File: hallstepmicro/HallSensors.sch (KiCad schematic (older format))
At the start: 16 parts

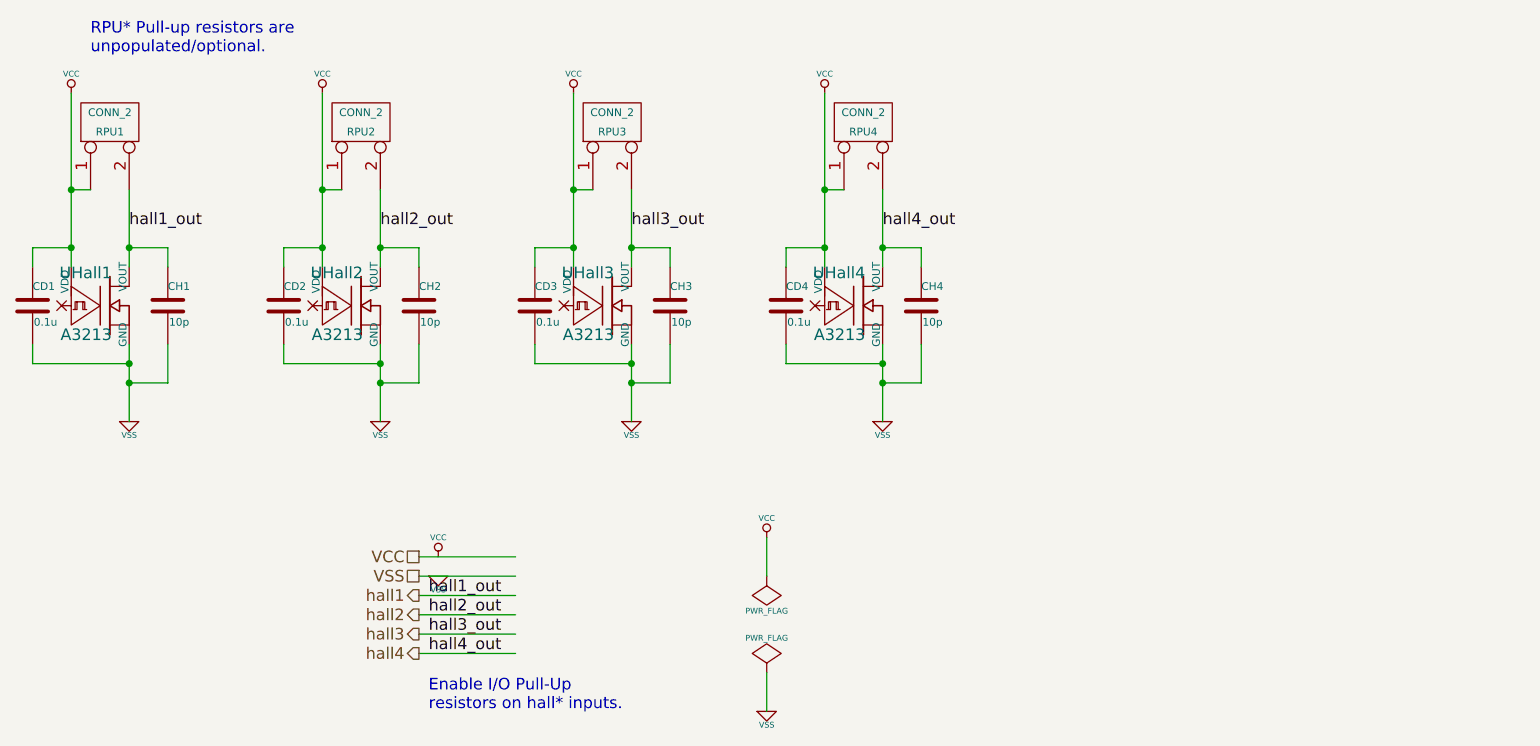
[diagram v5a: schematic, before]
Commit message: Adding some documentation & related markup.
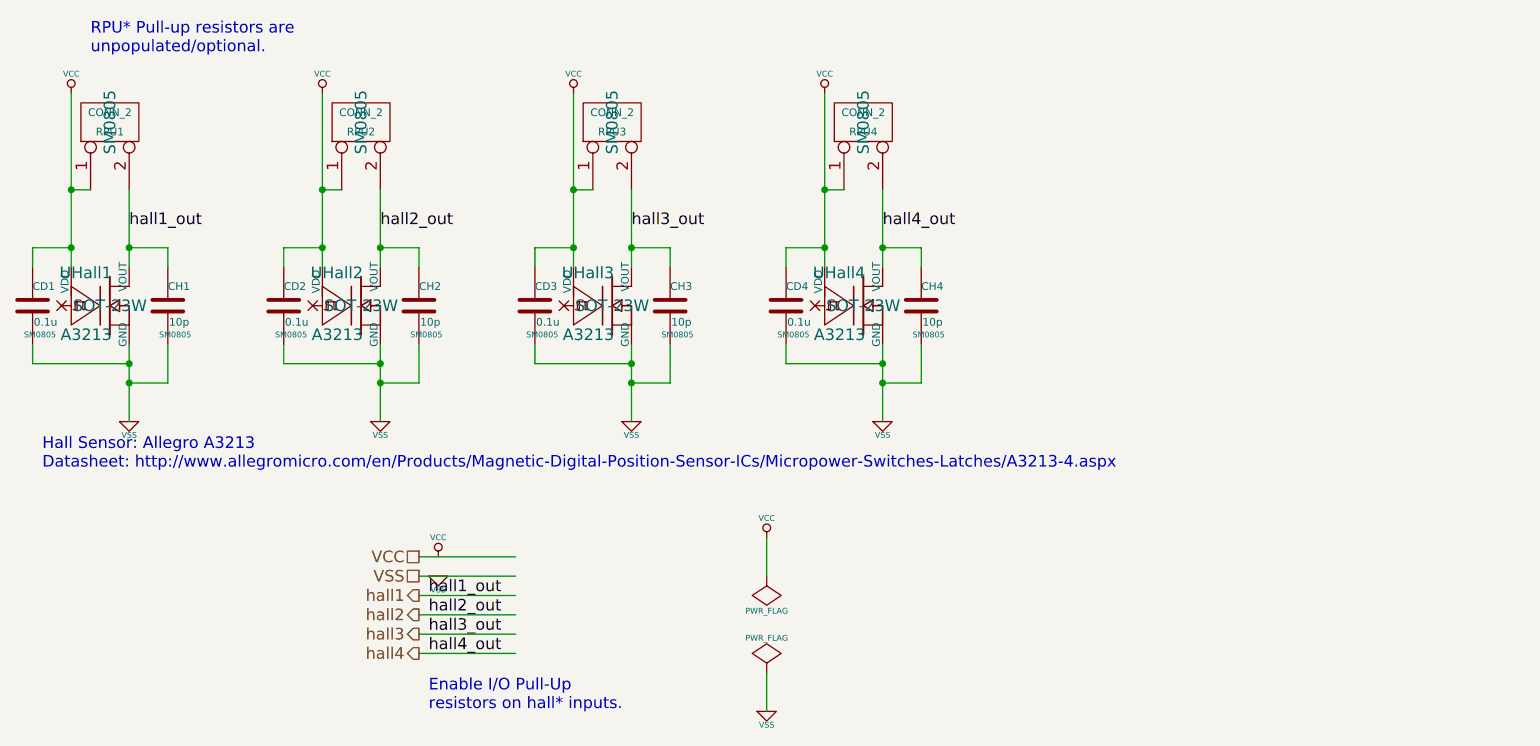
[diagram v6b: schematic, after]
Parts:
- CD1, CD2, CD3, CD4, CH1, CH2, CH3, CH4: footprint ~ -> SM0805
- RPU1, RPU2, RPU3, RPU4: footprint (none) -> SM0805
- UHall1, UHall2, UHall3, UHall4: footprint ~ -> SOT-23W
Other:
- note added: "Hall Sensor: Allegro A3213\nDatasheet: http://www.allegromicro.com/en/Products/Magnetic-Digital-Position-Sensor-ICs/Micropower-Switches-Latches/A3213-4.aspx"
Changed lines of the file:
@@
-EESchema Schematic File Version 2  date Wednesday, 02 October, 2013 09:18:38 pm
+EESchema Schematic File Version 2  date Friday, 04 October, 2013 11:24:01 am
 LIBS:power
 LIBS:device
@@
 encoding utf-8
 Sheet 2 2
-Title ""
-Date "3 oct 2013"
-Rev ""
-Comp ""
+Title "Hall Sensors With ATtiny84A Support"
+Date "4 oct 2013"
+Rev "20131004"
+Comp "ClothBot Designs"
 Comment1 ""
 Comment2 ""
@@
 F 0 "UHall1" H 1710 3670 60  0000 R CNN
 F 1 "A3213" H 1710 3350 60  0000 R CNN
-F 2 "~" H 1700 3500 60  0000 C CNN
-F 3 "~" H 1700 3500 60  0000 C CNN
+F 2 "SOT-23W" H 1700 3500 60  0000 C CNN
+F 3 "http://www.allegromicro.com/en/Products/Magnetic-Digital-Position-Sensor-ICs/Micropower-Switches-Latches/A3213-4.aspx" H 1700 3500 60  0001 C CNN
 	1    1700 3500
 	1    0    0    -1
@@
 F 0 "UHall2" H 3010 3670 60  0000 R CNN
 F 1 "A3213" H 3010 3350 60  0000 R CNN
-F 2 "~" H 3000 3500 60  0000 C CNN
-F 3 "~" H 3000 3500 60  0000 C CNN
+F 2 "SOT-23W" H 3000 3500 60  0000 C CNN
+F 3 "http://www.allegromicro.com/en/Products/Magnetic-Digital-Position-Sensor-ICs/Micropower-Switches-Latches/A3213-4.aspx" H 3000 3500 60  0001 C CNN
 	1    3000 3500
 	1    0    0    -1
@@
 F 0 "UHall3" H 4310 3670 60  0000 R CNN
 F 1 "A3213" H 4310 3350 60  0000 R CNN
-F 2 "~" H 4300 3500 60  0000 C CNN
-F 3 "~" H 4300 3500 60  0000 C CNN
+F 2 "SOT-23W" H 4300 3500 60  0000 C CNN
+F 3 "http://www.allegromicro.com/en/Products/Magnetic-Digital-Position-Sensor-ICs/Micropower-Switches-Latches/A3213-4.aspx" H 4300 3500 60  0001 C CNN
 	1    4300 3500
 	1    0    0    -1
@@
 F 0 "UHall4" H 5610 3670 60  0000 R CNN
 F 1 "A3213" H 5610 3350 60  0000 R CNN
-F 2 "~" H 5600 3500 60  0000 C CNN
-F 3 "~" H 5600 3500 60  0000 C CNN
+F 2 "SOT-23W" H 5600 3500 60  0000 C CNN
+F 3 "http://www.allegromicro.com/en/Products/Magnetic-Digital-Position-Sensor-ICs/Micropower-Switches-Latches/A3213-4.aspx" H 5600 3500 60  0001 C CNN
 	1    5600 3500
 	1    0    0    -1
@@
 F 0 "CD1" H 1300 3600 40  0000 L CNN
 F 1 "0.1u" H 1306 3415 40  0000 L CNN
-F 2 "~" H 1338 3350 30  0000 C CNN
+F 2 "SM0805" H 1338 3350 30  0000 C CNN
 F 3 "~" H 1300 3500 60  0000 C CNN
 	1    1300 3500
@@
 F 0 "CD2" H 2600 3600 40  0000 L CNN
 F 1 "0.1u" H 2606 3415 40  0000 L CNN
-F 2 "~" H 2638 3350 30  0000 C CNN
+F 2 "SM0805" H 2638 3350 30  0000 C CNN
 F 3 "~" H 2600 3500 60  0000 C CNN
 	1    2600 3500
@@
 F 0 "CD3" H 3900 3600 40  0000 L CNN
 F 1 "0.1u" H 3906 3415 40  0000 L CNN
-F 2 "~" H 3938 3350 30  0000 C CNN
+F 2 "SM0805" H 3938 3350 30  0000 C CNN
 F 3 "~" H 3900 3500 60  0000 C CNN
 	1    3900 3500
@@
 F 0 "CD4" H 5200 3600 40  0000 L CNN
 F 1 "0.1u" H 5206 3415 40  0000 L CNN
-F 2 "~" H 5238 3350 30  0000 C CNN
+F 2 "SM0805" H 5238 3350 30  0000 C CNN
 F 3 "~" H 5200 3500 60  0000 C CNN
 	1    5200 3500
@@
 F 0 "CH1" H 2000 3600 40  0000 L CNN
 F 1 "10p" H 2006 3415 40  0000 L CNN
-F 2 "~" H 2038 3350 30  0000 C CNN
+F 2 "SM0805" H 2038 3350 30  0000 C CNN
 F 3 "~" H 2000 3500 60  0000 C CNN
 	1    2000 3500
@@
 F 0 "CH2" H 3300 3600 40  0000 L CNN
 F 1 "10p" H 3306 3415 40  0000 L CNN
-F 2 "~" H 3338 3350 30  0000 C CNN
+F 2 "SM0805" H 3338 3350 30  0000 C CNN
 F 3 "~" H 3300 3500 60  0000 C CNN
 	1    3300 3500
@@
 F 0 "CH3" H 4600 3600 40  0000 L CNN
 F 1 "10p" H 4606 3415 40  0000 L CNN
-F 2 "~" H 4638 3350 30  0000 C CNN
+F 2 "SM0805" H 4638 3350 30  0000 C CNN
 F 3 "~" H 4600 3500 60  0000 C CNN
 	1    4600 3500
@@
 F 0 "CH4" H 5900 3600 40  0000 L CNN
 F 1 "10p" H 5906 3415 40  0000 L CNN
-F 2 "~" H 5938 3350 30  0000 C CNN
+F 2 "SM0805" H 5938 3350 30  0000 C CNN
 F 3 "~" H 5900 3500 60  0000 C CNN
 	1    5900 3500
@@
 F 0 "RPU1" V 1650 2550 40  0000 C CNN
 F 1 "CONN_2" V 1750 2550 40  0000 C CNN
-F 2 "" H 1700 2550 60  0000 C CNN
+F 2 "SM0805" H 1700 2550 60  0000 C CNN
 F 3 "" H 1700 2550 60  0000 C CNN
 	1    1700 2550
@@
 F 0 "RPU2" V 2950 2550 40  0000 C CNN
 F 1 "CONN_2" V 3050 2550 40  0000 C CNN
-F 2 "" H 3000 2550 60  0000 C CNN
-F 3 "" H 3000 2550 60  0000 C CNN
+F 2 "SM0805" H 3000 2550 60  0000 C CNN
+F 3 "http://www.allegromicro.com/en/Products/Magnetic-Digital-Position-Sensor-ICs/Micropower-Switches-Latches/A3213-4.aspx" H 3000 2550 60  0001 C CNN
 	1    3000 2550
 	0    -1   -1   0
@@
 F 0 "RPU3" V 4250 2550 40  0000 C CNN
 F 1 "CONN_2" V 4350 2550 40  0000 C CNN
-F 2 "" H 4300 2550 60  0000 C CNN
+F 2 "SM0805" H 4300 2550 60  0000 C CNN
 F 3 "" H 4300 2550 60  0000 C CNN
 	1    4300 2550
@@
 F 0 "RPU4" V 5550 2550 40  0000 C CNN
 F 1 "CONN_2" V 5650 2550 40  0000 C CNN
-F 2 "" H 5600 2550 60  0000 C CNN
+F 2 "SM0805" H 5600 2550 60  0000 C CNN
 F 3 "" H 5600 2550 60  0000 C CNN
 	1    5600 2550
@@
 Text Notes 1600 2200 0    60   ~ 0
 RPU* Pull-up resistors are\nunpopulated/optional.
+Text Notes 1350 4350 0    60   ~ 0
+Hall Sensor: Allegro A3213\nDatasheet: http://www.allegromicro.com/en/Products/Magnetic-Digital-Position-Sensor-ICs/Micropower-Switches-Latches/A3213-4.aspx
 $EndSCHEMATC
